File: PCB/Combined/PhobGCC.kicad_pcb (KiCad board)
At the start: 2 copper layers, 142.1 x 91.4 mm, 78 parts, among them J1 Conn_01x06_Female, J2 Conn_01x04_Female, J3 Conn_01x01_Male, J4 Conn_01x04_Male, J5 Conn_01x02_Male, Q1 Q_NMOS_GSD, Q2 Q_PMOS_GDS, Q3 Q_NMOS_GSD, SW1 A, SW10 Dup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

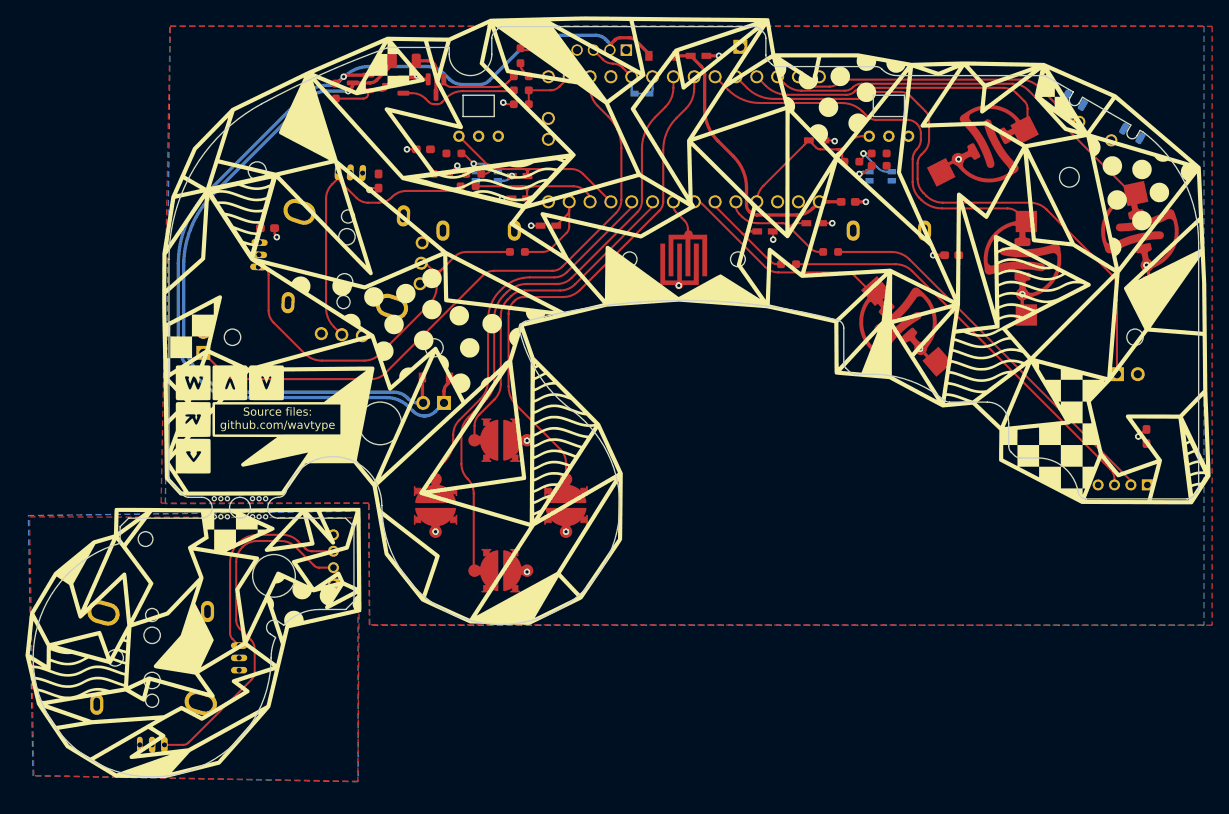
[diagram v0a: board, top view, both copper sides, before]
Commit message: rebuild for 1.2.1
added JST connector for rumble, button pinout, fixed outline, removed unused trigger sensors.
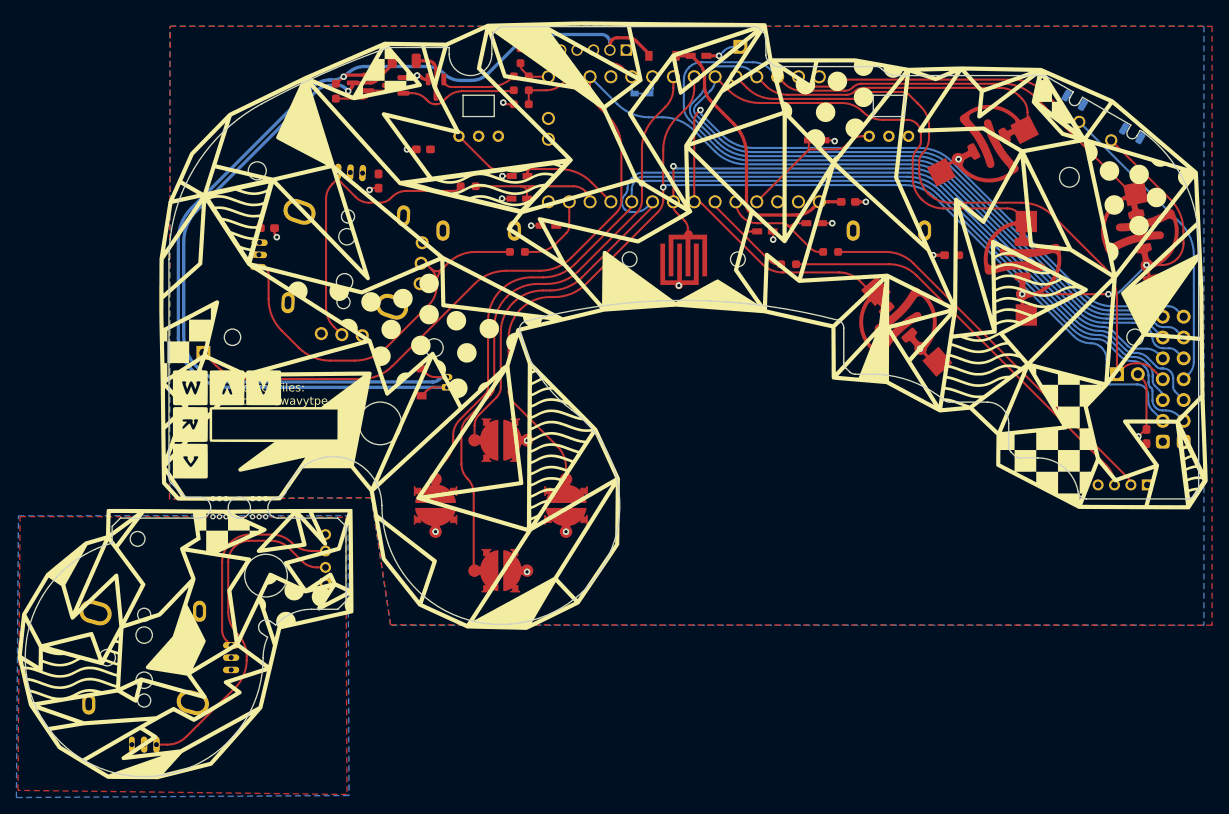
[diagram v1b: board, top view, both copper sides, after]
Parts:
- removed R10, R5, R6, R7, R8, R9: DNP, Resistor_SMD:R_0603_1608Metric_Pad0.98x0.95mm_HandSolder
- removed U3, U4: GP2S60-MFG, PhobGCC_Footprints:Sharp_Microelectronics-GP2S60-MFG
- removed cBS: LOGO, wavbrd_library:cstick_backsilk
- removed cFS: LOGO, wavbrd_library:cstick_silk
- removed mouse-bite-2.54mm-slot (x2): VAL**, agile_65:mouse-bite-2.54mm-slot
- removed wBS: LOGO, wavbrd_library:wavbrd_backsilk
- removed wFS: LOGO, wavbrd_library:wavbrd_silk
- added H14: MouseBite, wavbrd:mouse-bite-2.54mm-slot, F.Cu at (63.2, 107.4)
- added H15: MouseBite, wavbrd:mouse-bite-2.54mm-slot, F.Cu at (58.3, 107.4)
- added H16: MainFSilk, wavbrd:wavbrd_silk, F.Cu at (112.0, 86.2)
- added H17: MainBSilk, wavbrd:wavbrd_backsilk, F.Cu at (112.0, 86.2)
- added H18: CFSilk, wavbrd:cstick_silk, F.Cu at (51.6, 125.3)
- added H19: CBSilk, wavbrd:cstick_backsilk, F.Cu at (51.6, 125.3)
- added J6: Button_Out, wavbrd:PinSocket_2x07_P2.54mm_Vertical, B.Cu at (171.0, 85.4)
- C1, C2, C3, C4, C5, C6, C7: footprint Capacitors_SMD:C_0603_HandSoldering -> wavbrd:C_0603_HandSoldering
- C10, C11, C12, C13, C8, C9: footprint Capacitor_SMD:C_0603_1608Metric_Pad1.08x0.95mm_HandSolder -> wavbrd:C_0603_1608Metric_Pad1.08x0.95mm_HandSolder
- D1: footprint Gamecube MB:D_SOD-523_Shorted -> wavbrd:D_SOD-523_Shorted
- D2, D3: footprint Diode_SMD:D_SOD-123 -> wavbrd:D_SOD-123
- F1: footprint Resistor_SMD:R_1206_3216Metric -> wavbrd:R_1206_3216Metric
- H1, H11: footprint PhobGCC_Footprints:MountingHole_5.2mm -> wavbrd:MountingHole_5.2mm
- H10, H5, H6: footprint PhobGCC_Footprints:MountingHole_1.8mm -> wavbrd:MountingHole_1.8mm
- H12, H13, H3, H4: footprint PhobGCC_Footprints:MountingHole_2.0mm -> wavbrd:MountingHole_2.0mm
- H2: footprint PhobGCC_Footprints:Slot -> wavbrd:Slot
- H7: footprint PhobGCC_Footprints:MountingHole_2.4mm -> wavbrd:MountingHole_2.4mm
- H8, H9: footprint PhobGCC_Footprints:MountingHole_2.2mm -> wavbrd:MountingHole_2.2mm
- J1: footprint PhobGCC_Footprints:GCC_Header_Straight_1x06_Pitch2.00mm -> wavbrd:GCC_Header_Straight_1x06_Pitch2.00mm
- J2: footprint Pin_Headers:Pin_Header_Straight_1x04_Pitch2.00mm -> wavbrd:Pin_Header_Straight_1x04_Pitch2.00mm
- J3: footprint Connector_PinHeader_2.54mm:PinHeader_1x01_P2.54mm_Vertical -> wavbrd:PinHeader_1x01_P2.54mm_Vertical
- J4: footprint Connector_PinHeader_2.00mm:PinHeader_1x04_P2.00mm_Vertical -> wavbrd:PinHeader_1x04_P2.00mm_Vertical
- J5: footprint Connector_PinHeader_2.54mm:PinHeader_1x02_P2.54mm_Vertical -> Connector_Molex:Molex_PicoBlade_53048-0210_1x02_P1.25mm_Horizontal; moved to B.Cu
- Q1, Q2, Q3: footprint Package_TO_SOT_SMD:SOT-23 -> wavbrd:SOT-23
- R1, R11, R12, R13, R14, R15, R2, R3, R4: footprint Resistor_SMD:R_0603_1608Metric_Pad0.98x0.95mm_HandSolder -> wavbrd:R_0603_1608Metric_Pad0.98x0.95mm_HandSolder
- RV1, RV2: footprint PhobGCC_Footprints:GCC_Slider -> wavbrd:GCC_Slider
- SW1, SW2, SW3, SW4: footprint PhobGCC_Footprints:ABXY_Contact_Omron_Switch -> wavbrd:ABXY_Contact_Omron_Switch
- SW10, SW11, SW12, SW9: footprint PhobGCC_Footprints:Dpad_Contact_TL3315NF_2 -> wavbrd:Dpad_Contact_TL3315NF_2
- SW5: footprint PhobGCC_Footprints:Start_Contact -> wavbrd:Start_Contact
- SW6, SW7: footprint Pin_Headers:Pin_Header_Straight_1x02_Pitch2.54mm -> wavbrd:Pin_Header_Straight_1x02_Pitch2.54mm
- SW8: footprint PhobGCC_Footprints:Z_Switch_Edge -> wavbrd:Z_Switch_Edge
- U1: footprint teensy:Teensy40_Edge_Pins -> wavbrd:Teensy40_Edge_Pins
- U2: footprint PhobGCC_Footprints:GCC_Stickbox_2 -> wavbrd:GCC_Stickbox_2
- U5: footprint PhobGCC_Footprints:GCC_Stickbox_Hall_Only -> wavbrd:GCC_Stickbox_Hall_Only
- moved J5 1.93 mm to (83.8, 94.0), turned to 90 degrees
- moved D2 1.85 mm to (80.6, 93.4), turned to 90 degrees
- moved H11 0.97 mm to (61.7, 117.0)
- moved H12 0.97 mm to (42.3, 127.0)
- moved H13 0.97 mm to (51.3, 127.0)
- moved J4 0.97 mm to (68.9, 118.0)
- moved U5 0.97 mm to (46.8, 127.0)
- moved H10 0.97 mm to (46.0, 112.5)
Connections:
- SW8 pad 3: (no net) -> unconnected-(SW8-Pad3)
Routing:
- net /X: track 49.8 -> 135.7 mm
- net /Dup: track 41.2 -> 126.8 mm
- net /L: track 77.5 -> 162.5 mm
- net /Y: track 36.6 -> 119.5 mm
- net /B: track 26.6 -> 106.5 mm, vias 0 -> 1
- net /Dleft: track 46.1 -> 125.0 mm
- net /Ddown: track 73.5 -> 152.3 mm, vias 0 -> 1
- net /Dright: track 64.1 -> 137.9 mm, vias 0 -> 1
- net /Start: track 4.47 -> 77.4 mm, vias 0 -> 1
- net /A: track 49.2 -> 120.9 mm
- net GND: track 23.7 -> 71.5 mm, vias 24 -> 25
- net /Z: track 36.8 -> 74.0 mm
- net Net-(R6-Pad2): track 6.65 -> 0.00 mm, vias 1 -> 0
- net Net-(R10-Pad2): track 6.48 -> 0.00 mm, vias 1 -> 0
- net /R: track 74.9 -> 79.6 mm
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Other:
- board size 142.1 x 91.4 mm -> 143 x 91.4 mm
- board text added: "Source files: github.com/wavytpe"
- board text removed: "Source files: github.com/wavtype"
